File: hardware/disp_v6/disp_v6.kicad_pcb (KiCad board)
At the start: 2 copper layers, 130 x 70 mm, 241 parts, among them J1 RJ45, J12 Conn_01x06, J2 Conn_01x06_Pin, J3 Conn_01x05_Pin, J4 Conn_01x04_Pin, J5 Conn_01x06_Pin, J6 Conn_01x04_Pin, J7 Conn_01x04_Pin, J8 Conn_01x02, J9 Conn_02x10_Odd_Even, Q1 2N7002, Q10 2N7002, Q2 2N7002, Q3 2N7002, Q4 2N7002, Q5 2N7002, Q6 2N7002, Q7 2N7002, Q8 2N7002, Q9 2N7002, U1 ADA4807-1, U10 STM32F405RGTx, U11 AMS1117-3.3, U12 BA50DD0WHFP-TR, U13 M24C02-RMN, U2 SN74LVC1G14DBV, U3 SN74LVC1G14DBV, U4 ADA4807-1, U5 ADA4807-1, U6 TLV3603DCKR, U7 SN74LVC1G14DBV, U8 TLV3603DCKR, U9 L78L05_SOT89, X2 GTXO-14V (2.048MHz), Y1 AOCJY4A-10.000MHZ-SW, Y2 16MHz

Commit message: start clean up of disp 6
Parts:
- removed ANT1, ANT2, ANT3, ANT4, ANT5, ANT6: U.FL-R-SMT-1, blinky_footprints:U.FL-R-SMT-1
- removed C1, C10, C11, C17, C18, C2, C25, C26, C30, C33, C45, C46, C47, C48, C49, C9: 100nF, Capacitor_SMD:C_0402_1005Metric
- removed C12, C14, C19, C23, C5, C7: 150pF, Capacitor_SMD:C_0603_1608Metric
- removed C13, C20, C8: 330pF, Capacitor_SMD:C_0603_1608Metric
- removed C15, C22, C6: 220pF, Capacitor_SMD:C_0603_1608Metric
- removed C16, C21, C3: 1nF, Capacitor_SMD:C_0603_1608Metric
- removed C24, C27, C37: 100nF, Capacitor_SMD:C_0603_1608Metric
- removed C28, C29: 33pF, Capacitor_SMD:C_0603_1608Metric
- removed C34, C43: 10uF, Capacitor_Tantalum_SMD:CP_EIA-3216-18_Kemet-A
- removed C35, C40: 2.2uF, Capacitor_SMD:C_0603_1608Metric
- removed C4: 47pF, Capacitor_SMD:C_0805_2012Metric
- removed C42, C44: 33uF, Capacitor_Tantalum_SMD:CP_EIA-3528-21_Kemet-B
- removed FB1: 120Ω@100MHz, Resistor_SMD:R_0603_1608Metric
- removed H3: M2, MountingHole:MountingHole_2.2mm_M2
- removed J1: RJ45, Connector_RJ:RJ45_Amphenol_RJHSE5380
- removed J12: Conn_01x06, Connector_JST:JST_PH_S6B-PH-SM4-TB_1x06-1MP_P2.00mm_Horizontal
- removed J2, J5: Conn_01x06_Pin, Connector_PinHeader_2.54mm:PinHeader_1x06_P2.54mm_Vertical
- removed J3: Conn_01x05_Pin, Connector_PinHeader_2.54mm:PinHeader_1x05_P2.54mm_Vertical
- removed J4, J6, J7: Conn_01x04_Pin, Connector_PinHeader_2.54mm:PinHeader_1x04_P2.54mm_Vertical
- removed J8: Conn_01x02, Connector_JST:JST_PH_S2B-PH-SM4-TB_1x02-1MP_P2.00mm_Horizontal
- removed JP1: SolderJumper_2_Bridged, Jumper:SolderJumper-2_P1.3mm_Bridged_RoundedPad1.0x1.5mm
- removed L1, L2, L3, L4, L5, L6: 1uF, Inductor_SMD:L_0805_2012Metric
- removed R1, R15, R16: 100R, Resistor_SMD:R_0603_1608Metric
- removed R10, R2, R6: 510R, Resistor_SMD:R_0603_1608Metric
- removed R11, R3, R7: 49R9, Resistor_SMD:R_0603_1608Metric
- removed R12, R13: 1K5, Resistor_SMD:R_0805_2012Metric
- removed R14: 330R, Resistor_SMD:R_0805_2012Metric
- removed R17: 20R, Resistor_SMD:R_0805_2012Metric
- removed R18, R21: 130K, Resistor_SMD:R_0603_1608Metric
- removed R19, R20, R22, R24, R5, R54, R60, R61, R62, R63, R64: 1K0, Resistor_SMD:R_0603_1608Metric
- removed R23: 22K, Resistor_SMD:R_0805_2012Metric
- removed R25: 270R, Resistor_SMD:R_0603_1608Metric
- removed R26: 22R0, Resistor_SMD:R_0603_1608Metric
- removed R27, R28, R32: 4K7, Resistor_SMD:R_0603_1608Metric
- removed R4: 200R, Resistor_SMD:R_0805_2012Metric
- removed R58, R59: 1K5, Resistor_SMD:R_0603_1608Metric
- removed R8: 270R, Resistor_SMD:R_0805_2012Metric
- removed R9: 2R, Resistor_SMD:R_0805_2012Metric
- removed RV1: 20K, Potentiometer_SMD:Potentiometer_Bourns_3314G_Vertical
- removed S1, S2: 147873-2, blinky_footprints:SW_147873-2
- removed TP1, TP10, TP11, TP12, TP13, TP14, TP15, TP16, TP18, TP19, TP2, TP3, TP4, TP5, TP6, TP7, TP8, TP9: ~, TestPoint:TestPoint_THTPad_D1.5mm_Drill0.7mm
- removed U1, U4, U5: ADA4807-1, Package_TO_SOT_SMD:SOT-23-6
- removed U10: STM32F405RGTx, Package_QFP:LQFP-64_10x10mm_P0.5mm
- removed U12: BA50DD0WHFP-TR, blinky_footprints:DPAK172P1054X200-6N
- removed U13: M24C02-RMN, Package_SO:SOIC-8_3.9x4.9mm_P1.27mm
- removed U2, U3, U7: SN74LVC1G14DBV, Package_TO_SOT_SMD:SOT-23-5
- removed U6, U8: TLV3603DCKR, blinky_footprints:SC70_DCK_TEX
- removed U9: L78L05_SOT89, Package_TO_SOT_SMD:SOT-89-3
- removed X2: GTXO-14V (2.048MHz), Oscillator:Oscillator_DIP-14
- removed Y1: AOCJY4A-10.000MHZ-SW, blinky_footprints:XTAL_AOCJY4A-10.000MHZ-SW
- removed Y2: 16MHz, Crystal:Crystal_SMD_3225-4Pin_3.2x2.5mm
- moved TP17 216.2 mm to (1.27, 1.27)
- moved C32 35.4 mm to (194.2, 47.7)
- moved C36 34.3 mm to (189.1, 47.2)
- moved H1 30.7 mm to (93.0, 45.5)
- moved H5 27.1 mm to (91.3, 123.9)
- moved C38 20.7 mm to (184.1, 47.2)
- moved H4 15.3 mm to (236.2, 128.6)
- moved C31 15.3 mm to (178.2, 47.4)
- moved H2 9.24 mm to (233.6, 46.4)
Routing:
- net GND: track 1188.4 -> 699.9 mm, vias 59 -> 15
- net +3.3V: track 408.1 -> 100.4 mm, vias 17 -> 4
- net +3.3VA: track 229.6 -> 0.00 mm, vias 9 -> 0
- net +6V: track 211.6 -> 2.70 mm, vias 7 -> 0
- net SYNC_OUT: track 125.6 -> 0.00 mm, vias 5 -> 0
- net +5V: track 122.2 -> 0.00 mm, vias 4 -> 0
- net +5VA: track 112.9 -> 0.00 mm, vias 6 -> 0
- net OSC_ADJ: track 107.4 -> 0.00 mm, vias 6 -> 0
- net /GPS_TX1: track 105.7 -> 0.00 mm, vias 3 -> 0
- net /GPS_RX1: track 98.1 -> 0.00 mm, vias 2 -> 0
- net SYNC_IN: track 88.7 -> 0.00 mm, vias 2 -> 0
- net SYNC_IN2: track 86.2 -> 0.00 mm, vias 2 -> 0
- net AUX_CLK: track 77.2 -> 0.00 mm, vias 4 -> 0
- net /GPS_EXT_PPS: track 76.2 -> 0.00 mm, vias 2 -> 0
- net /AUD_OUT: track 73.5 -> 0.00 mm, vias 2 -> 0
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- removed copper zone on F.Cu, net GND
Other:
- board text removed: "3.3V"
- board text removed: "3.3VA"
- board text removed: "5V"
- board text removed: "5VA"
- board text removed: "6V Power"
- board text removed: "Boot0"
- board text removed: "CH1"
- board text removed: "CH2"
- board text removed: "CH3"
- board text removed: "FrqAdj"
- board text removed: "GPS"
- board text removed: "GpsPps"
- board text removed: "I2C"
- board text removed: "NRst"
- board text removed: "OscIn"
- board text removed: "OscM"
- board text removed: "RX/TX"
- board text removed: "SIn"
- board text removed: "SOut"
- board text removed: "SWD"

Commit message: first route of disp board
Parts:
- removed C31, C39: 100nF, Capacitor_SMD:C_0402_1005Metric
- removed C41: 10uF, Capacitor_Tantalum_SMD:CP_EIA-3216-18_Kemet-A
- removed J9: Conn_02x10_Odd_Even, Connector_PinHeader_2.54mm:PinHeader_2x10_P2.54mm_Vertical
- removed TP17: ~, TestPoint:TestPoint_THTPad_D1.5mm_Drill0.7mm
- removed U11: AMS1117-3.3, Package_TO_SOT_SMD:SOT-223-3_TabPin2
- added J1: Conn_02x16_Odd_Even, Connector_PinHeader_2.54mm:PinHeader_2x16_P2.54mm_Vertical, B.Cu at (233.0, 76.0)
- added Q11: 2N7002, Package_TO_SOT_SMD:SOT-23, F.Cu at (237.7, 98.3)
- D1: value LED-RED -> LED-R
- moved H1 84.0 mm to (172.8, 71.6)
- moved H5 81.5 mm to (172.5, 116.6)
- moved C38 74.9 mm to (214.7, 115.6), turned to -90 degrees
- moved Q9 72.0 mm to (237.7, 94.5), turned to 180 degrees
- moved Q10 70.7 mm to (237.7, 90.9), turned to 180 degrees
- moved R31 65.2 mm to (234.2, 94.6), turned to -90 degrees
- moved R29 61.5 mm to (232.3, 94.6), turned to -90 degrees
- moved R30 57.6 mm to (230.2, 94.6), turned to -90 degrees
- moved D3 55.1 mm to (225.9, 87.1), turned to 90 degrees
- moved C32 55.0 mm to (241.8, 75.1), turned to 90 degrees
- moved C36 53.4 mm to (228.4, 83.2), turned to 90 degrees
- moved D2 51.3 mm to (223.9, 87.2), turned to 90 degrees
- moved D1 47.2 mm to (221.9, 87.2), turned to 90 degrees
- moved H2 28.7 mm to (247.1, 71.8)
- moved Q5 20.0 mm to (181.7, 111.2)
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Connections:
- R30 pad 2: /LEDM2 -> Net-(Q11-D)
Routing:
- net GND: track 699.9 -> 264.7 mm, vias 15 -> 14
- net /LEDM2: track 0.00 -> 85.9 mm
- net /LEDM1: track 0.00 -> 70.0 mm
- net /LEDM3: track 0.00 -> 60.8 mm
- net /LEDB: track 65.5 -> 109.9 mm, vias 1 -> 2
- net /LEDA: track 35.9 -> 76.9 mm, vias 1 -> 2
- net /LEDD: track 59.9 -> 99.1 mm, vias 1 -> 2
- net /LEDC: track 54.8 -> 92.2 mm, vias 1 -> 2
- net /LEDG: track 37.7 -> 74.8 mm, vias 1 -> 2
- net /LEDF: track 48.1 -> 83.9 mm, vias 1 -> 2
- net /LEDE: track 48.5 -> 83.5 mm, vias 1 -> 2
- net /LD: track 53.6 -> 24.8 mm
- net /LF: track 51.0 -> 22.8 mm
- net /LB: track 56.4 -> 28.7 mm
- net /LA: track 47.7 -> 21.7 mm
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- removed copper zone on F.Cu, net +3.3V
- removed copper zone on B.Cu, net GND
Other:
- board size 130 x 70 mm -> 82 x 52 mm
- board text added: "Disp Rev6.0 Cullen Jennings"
- board text removed: "Blinky Rev5.0 Cullen Jennings"

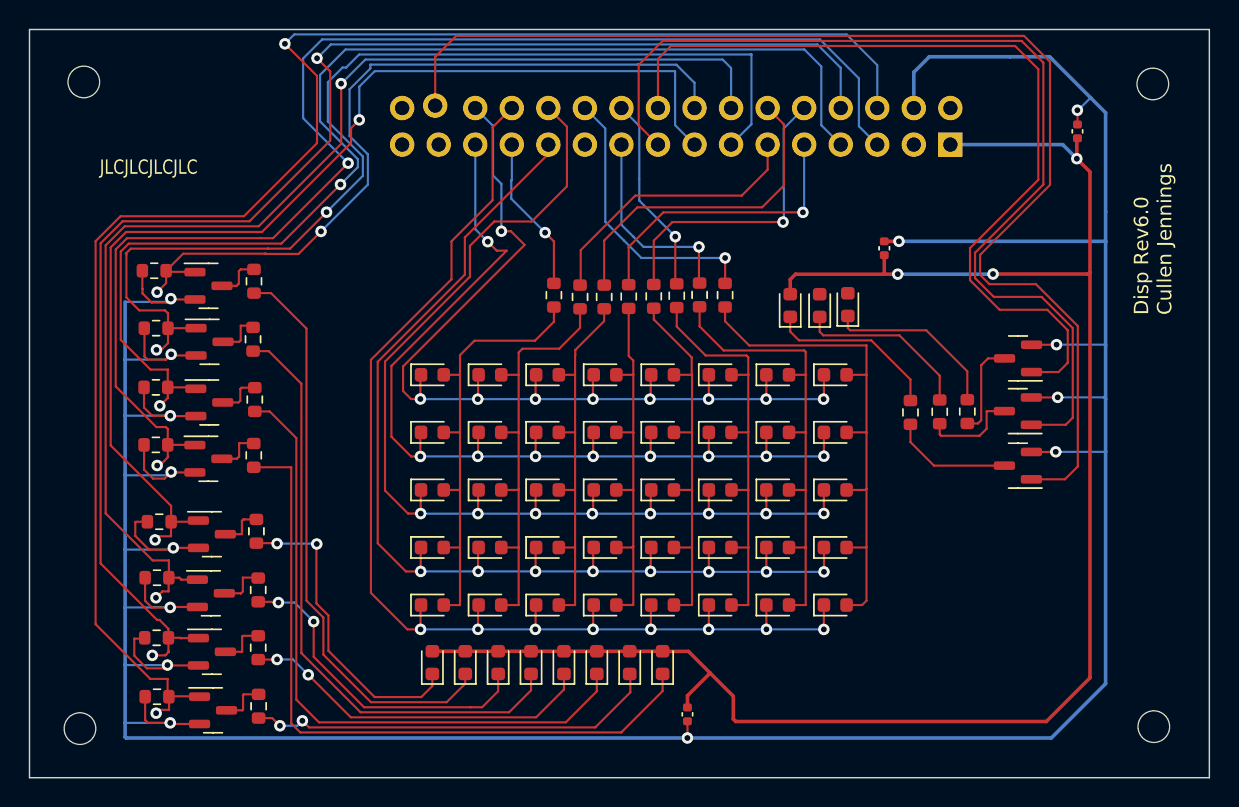
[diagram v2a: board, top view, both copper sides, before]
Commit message: clean up disp layout
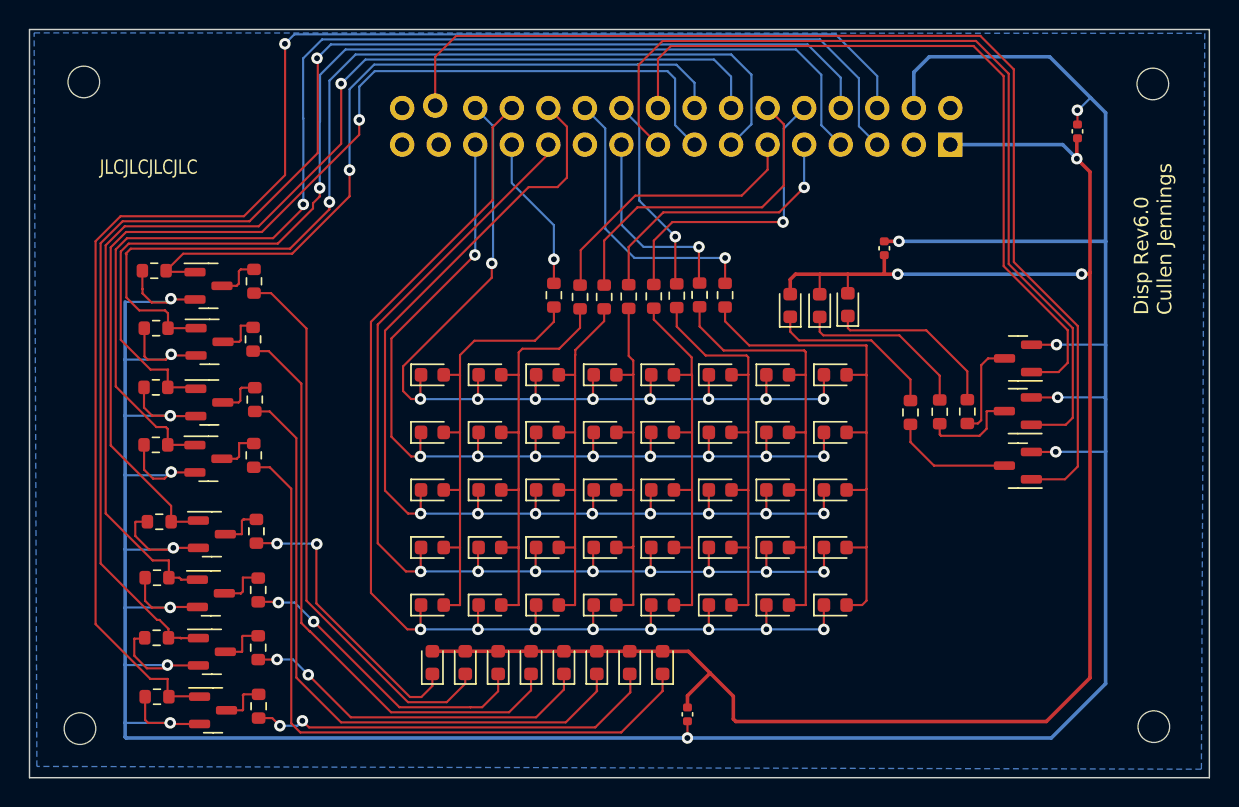
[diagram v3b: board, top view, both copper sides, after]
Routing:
- net /LEDM1: track 70.0 -> 62.3 mm
- net /LEDM2: track 85.9 -> 78.2 mm
- net /LEDM3: track 60.8 -> 53.2 mm
- net /LEDG: track 74.8 -> 69.9 mm, vias 2 -> 1
- net /LEDC: track 92.2 -> 87.4 mm, vias 2 -> 1
- net /LEDB: track 109.9 -> 105.7 mm, vias 2 -> 1
- net /LEDE: track 83.5 -> 79.3 mm, vias 2 -> 1
- net /LEDD: track 99.1 -> 95.7 mm, vias 2 -> 1
- net /LEDH: track 54.7 -> 51.4 mm, vias 2 -> 1
- net +3.3V: track 123.4 -> 126.2 mm
- net /LEDA: track 76.9 -> 74.3 mm, vias 2 -> 1
- net /LEDF: track 83.9 -> 81.6 mm, vias 2 -> 1
- net /COL1: track 68.9 -> 66.7 mm
- net /COL2: track 68.0 -> 65.8 mm
- net /LH: track 40.3 -> 38.7 mm
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- added copper zone on B.Cu, net GND

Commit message: update
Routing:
- net /ROW8: track 19.9 -> 22.3 mm
- net /ROW4: track 19.5 -> 21.3 mm
- net /ROW2: track 19.5 -> 20.8 mm
- net /ROW3: track 23.0 -> 24.1 mm
- net /ROW7: track 14.1 -> 15.2 mm
- net /ROW6: track 13.8 -> 14.6 mm
- net /ROW1: track 21.1 -> 21.6 mm

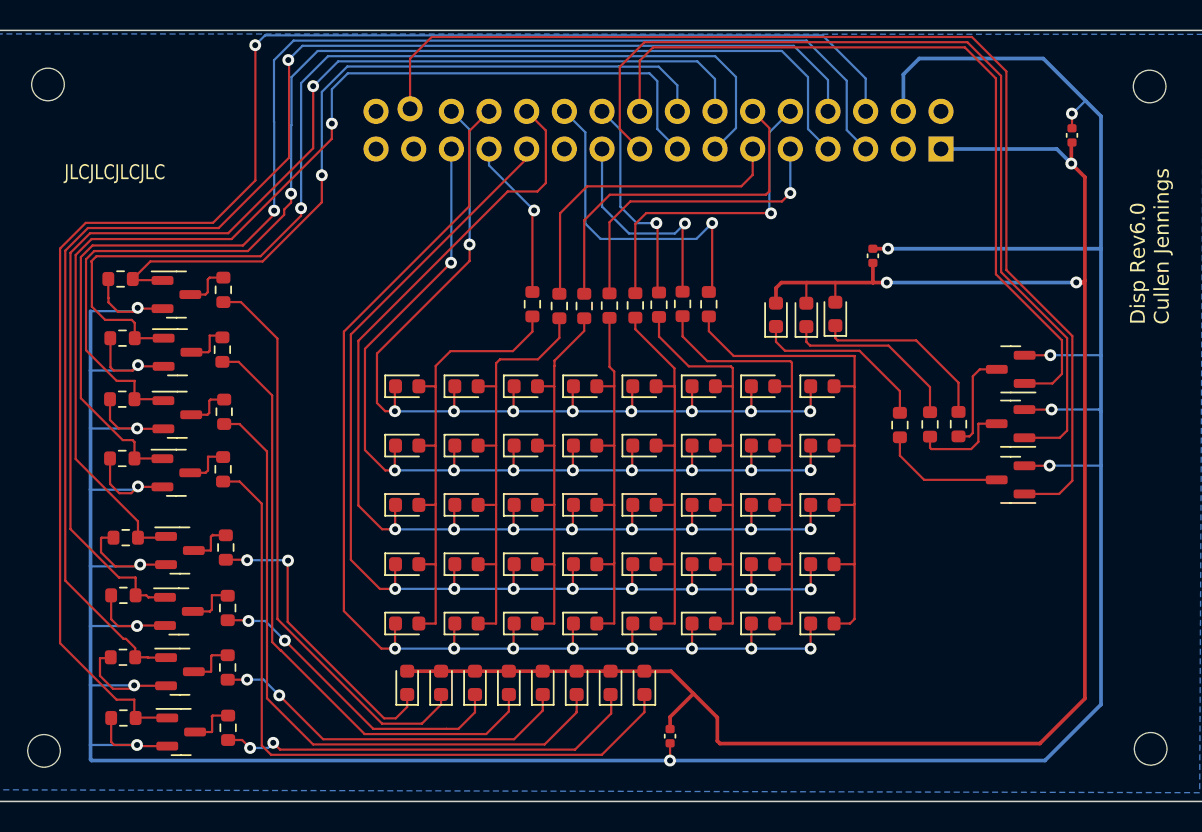
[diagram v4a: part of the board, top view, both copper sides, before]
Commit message: add two more rows of grid lights
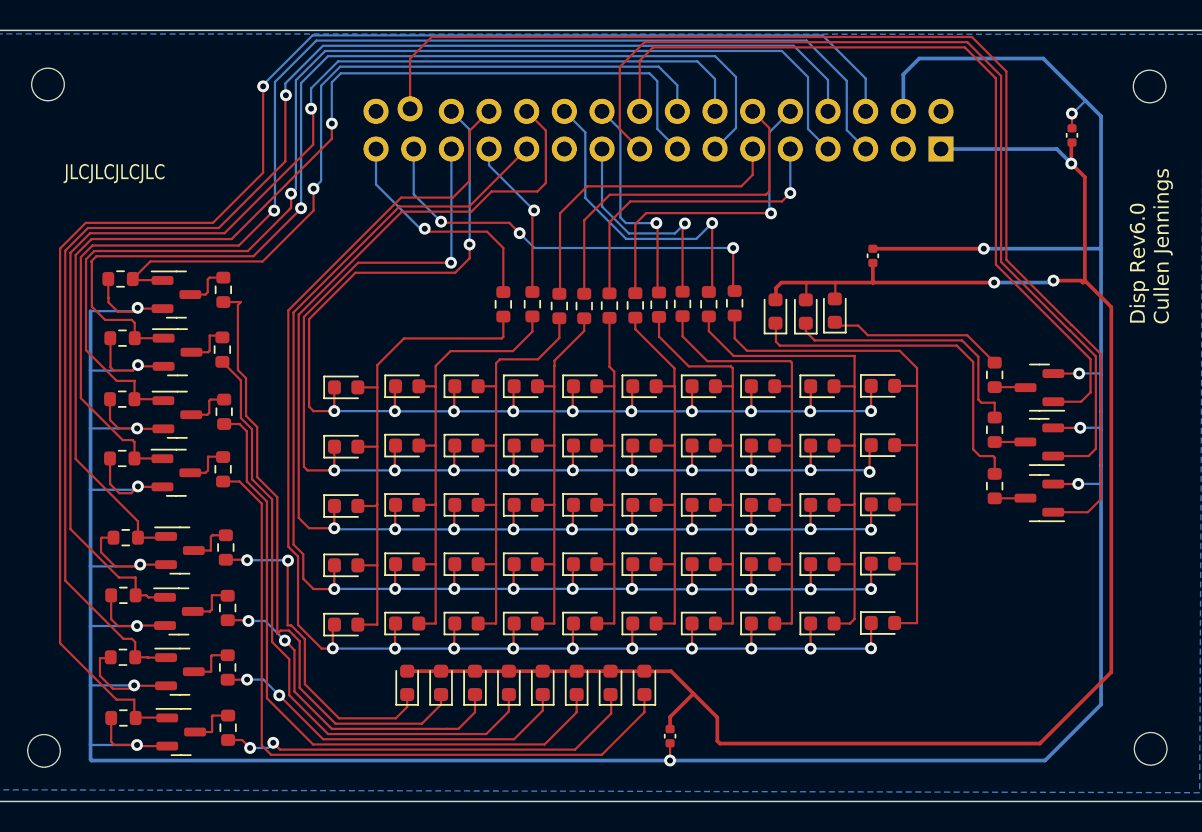
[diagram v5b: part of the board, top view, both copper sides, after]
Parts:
- added D52: LED-G, LED_SMD:LED_0603_1608Metric, F.Cu at (192.9, 96.1)
- added D53: LED-G, LED_SMD:LED_0603_1608Metric, F.Cu at (192.9, 92.1)
- added D54: LED-G, LED_SMD:LED_0603_1608Metric, F.Cu at (192.9, 108.1)
- added D55: LED-G, LED_SMD:LED_0603_1608Metric, F.Cu at (192.9, 100.1)
- added D56: LED-G, LED_SMD:LED_0603_1608Metric, F.Cu at (192.9, 104.1)
- added D57: LED-G, LED_SMD:LED_0603_1608Metric, F.Cu at (229.1, 96.0)
- added D58: LED-G, LED_SMD:LED_0603_1608Metric, F.Cu at (229.1, 92.0)
- added D59: LED-G, LED_SMD:LED_0603_1608Metric, F.Cu at (229.1, 108.0)
- added D60: LED-G, LED_SMD:LED_0603_1608Metric, F.Cu at (229.1, 100.0)
- added D61: LED-G, LED_SMD:LED_0603_1608Metric, F.Cu at (229.1, 104.0)
- added R1: 82R, Resistor_SMD:R_0603_1608Metric, F.Cu at (203.5, 86.5)
- added R2: 82R, Resistor_SMD:R_0603_1608Metric, F.Cu at (219.1, 86.4)
- moved R30 7.61 mm to (236.6, 98.7)
- moved R29 4.38 mm to (236.6, 94.9)
- moved R31 4.12 mm to (236.6, 91.2)
- moved Q11 2.30 mm to (239.6, 99.5)
- moved Q9 2.30 mm to (239.6, 95.8)
- moved Q10 2.30 mm to (239.6, 92.1)
- moved D1 0.23 mm to (221.8, 87.0)
- moved D3 0.23 mm to (225.8, 86.9)
- moved D2 0.23 mm to (223.9, 87.0)
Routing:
- net /R0: track 0.00 -> 39.5 mm
- net /R9: track 0.00 -> 34.8 mm
- net /AUX_CLK: track 0.00 -> 29.0 mm, vias 0 -> 3
- net /COL2: track 65.8 -> 83.8 mm, vias 9 -> 11
- net /COL1: track 66.7 -> 84.4 mm, vias 9 -> 11
- net /COL4: track 77.9 -> 94.8 mm, vias 8 -> 10
- net /COL5: track 77.9 -> 93.8 mm, vias 8 -> 10
- net /AUX_GPS_PPS: track 0.00 -> 15.7 mm, vias 0 -> 1
- net /COL3: track 83.8 -> 98.8 mm, vias 8 -> 10
- net Net-(D1-K): track 12.2 -> 23.6 mm
- net Net-(Q11-D): track 8.44 -> 2.08 mm
- net GND: track 264.3 -> 258.6 mm
- net Net-(D2-K): track 12.3 -> 18.0 mm
- net Net-(Q9-D): track 6.69 -> 2.07 mm
- net Net-(Q10-D): track 6.70 -> 2.10 mm
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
